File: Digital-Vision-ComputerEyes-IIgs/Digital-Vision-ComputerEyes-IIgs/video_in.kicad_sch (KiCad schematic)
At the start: 47 parts, among them J1 CAPTURE_IN, J2 MONITOR_OUT, J3 MONITOR_IN, Q1 2N3904, Q2 2N3906, Q3 2N3904, U1 74HCT4053, U7 TDA3330, Y1 3.579545 MHz

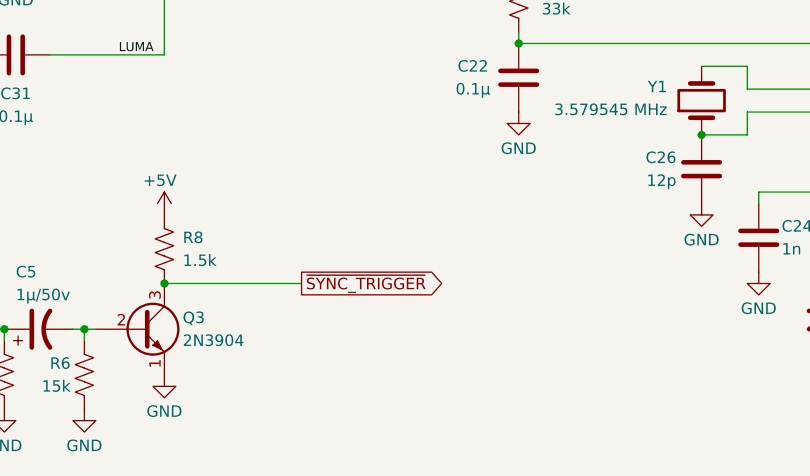
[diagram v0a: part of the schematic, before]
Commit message: Add some more details on ComputerEyes operation
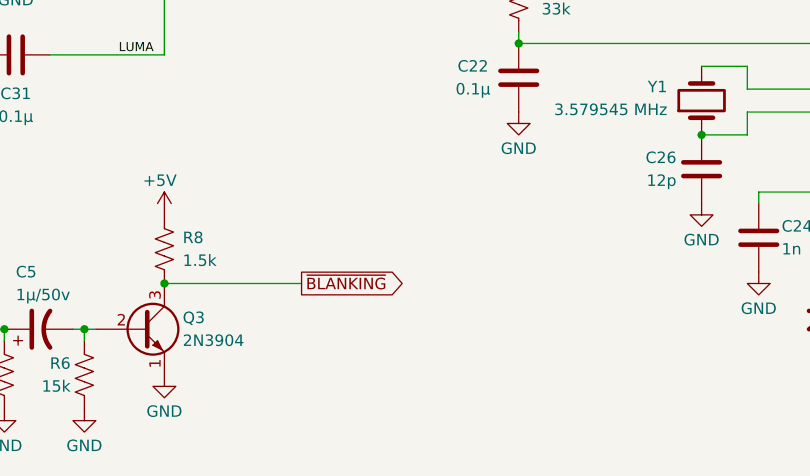
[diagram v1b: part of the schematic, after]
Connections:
- net ~{SYNC_TRIGGER} renamed ~{BLANKING}
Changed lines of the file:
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@@
 		)
 	)
-	(global_label "~{SYNC_TRIGGER}"
+	(global_label "~{BLANKING}"
 		(shape output)
 		(at 179.07 176.53 0)
@@
 		)
 		(property "Intersheetrefs" "${INTERSHEET_REFS}"
-			(at 195.7228 176.53 0)
+			(at 191.2477 176.53 0)
 			(effects
 				(font
